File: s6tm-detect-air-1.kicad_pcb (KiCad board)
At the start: 2 copper layers, 67 x 67 mm, 82 parts, among them J1 Conn_01x04, J2 TC2030, J3 Conn_01x04, J4 Conn_01x04, J5 Conn_01x04_Pin, J6 Conn_01x08, SW1 SW_Push, SW2 SW_Push, U1 SYS1002-H2, U10 004-1-0100, U2 MiCS-5524, U3 LMC6482, U4 HT753-1, U5 SN65HVD230, U6 STM32F103C8Tx, U7 HTU21, U8 LM73100, U9 ENS16x, Y1 8M

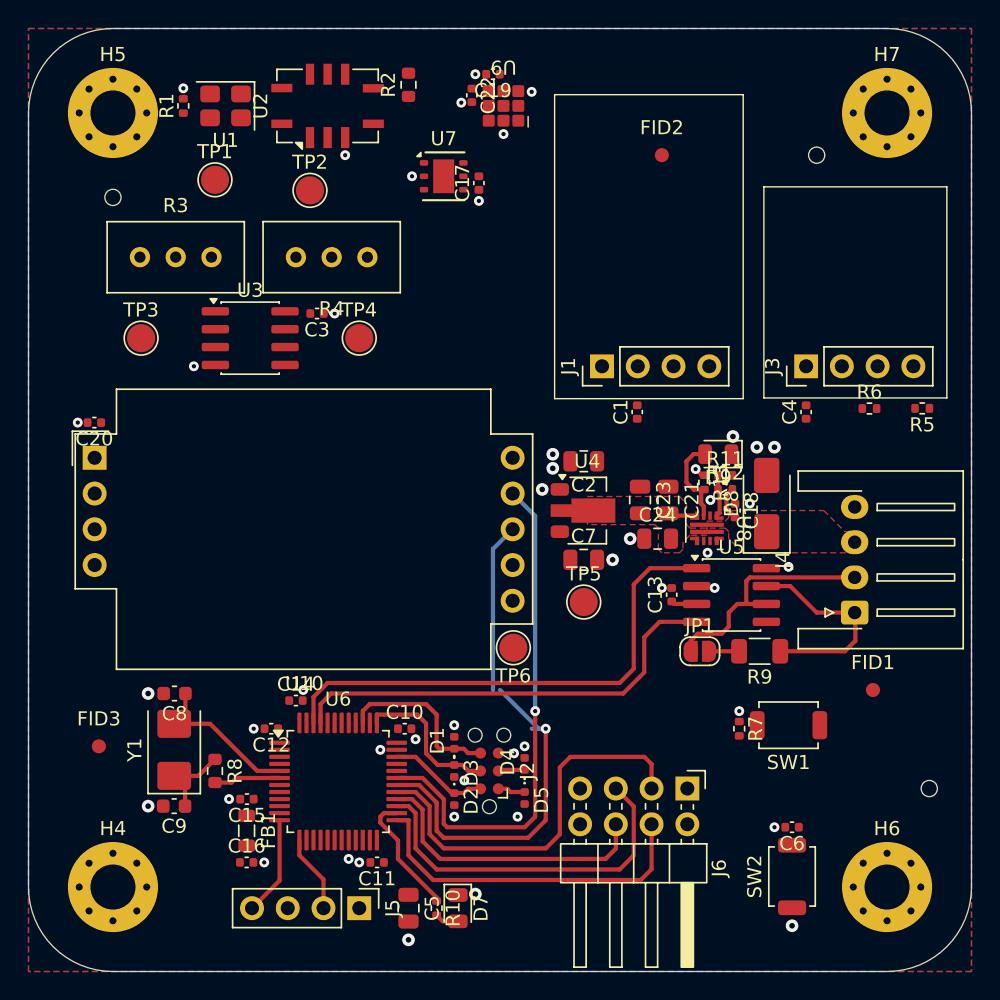
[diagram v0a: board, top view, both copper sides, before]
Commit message: pcb: add s88 cutout
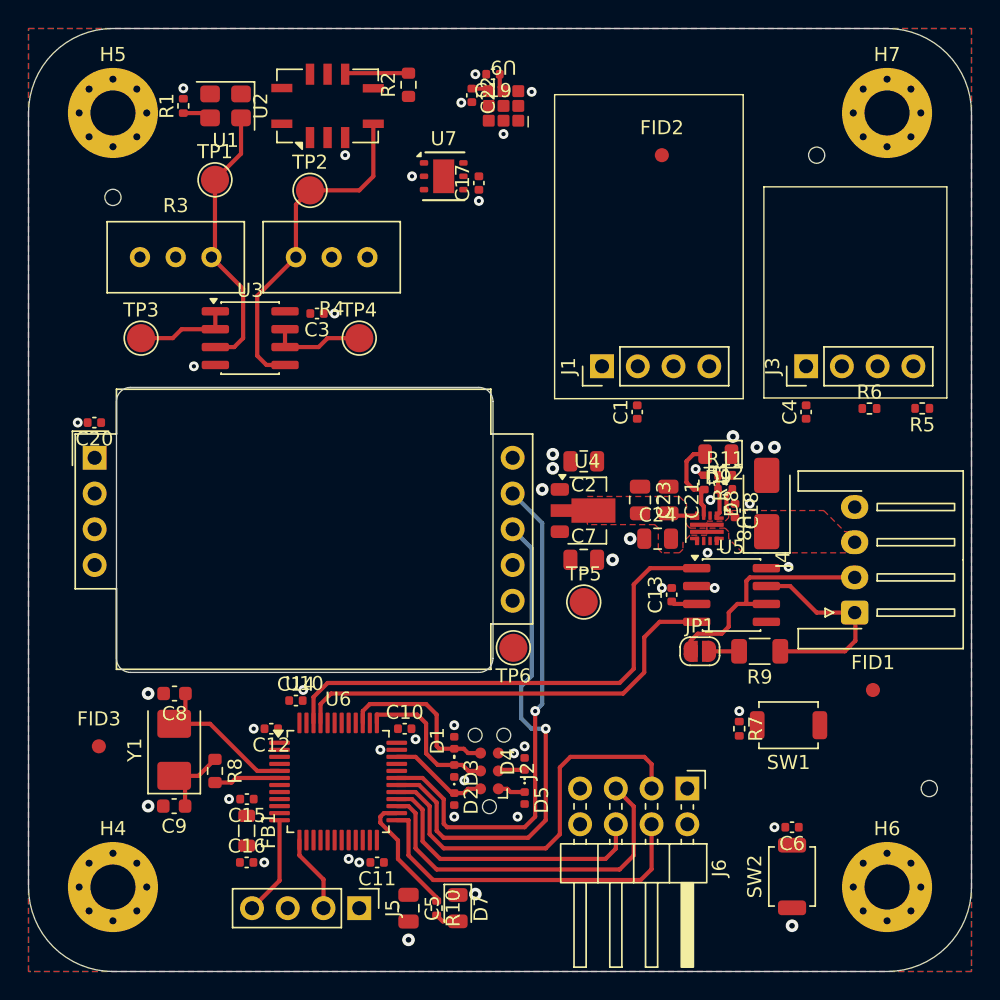
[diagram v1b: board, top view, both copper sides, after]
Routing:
- net Net-(U2-Rs1): track 0.00 -> 24.2 mm
- net Net-(U1-RS2): track 0.00 -> 19.7 mm
- net /RS_1: track 0.00 -> 6.81 mm
- net /RS_2: track 0.00 -> 6.81 mm
- net Net-(U2-Rh2): track 0.00 -> 4.53 mm
- net +3V3: track 4.60 -> 7.18 mm
- net Net-(U1-RH2): track 0.00 -> 2.04 mm
- net /S88_TX: track 37.2 -> 36.7 mm
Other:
- outline, holes or cut-outs redrawn

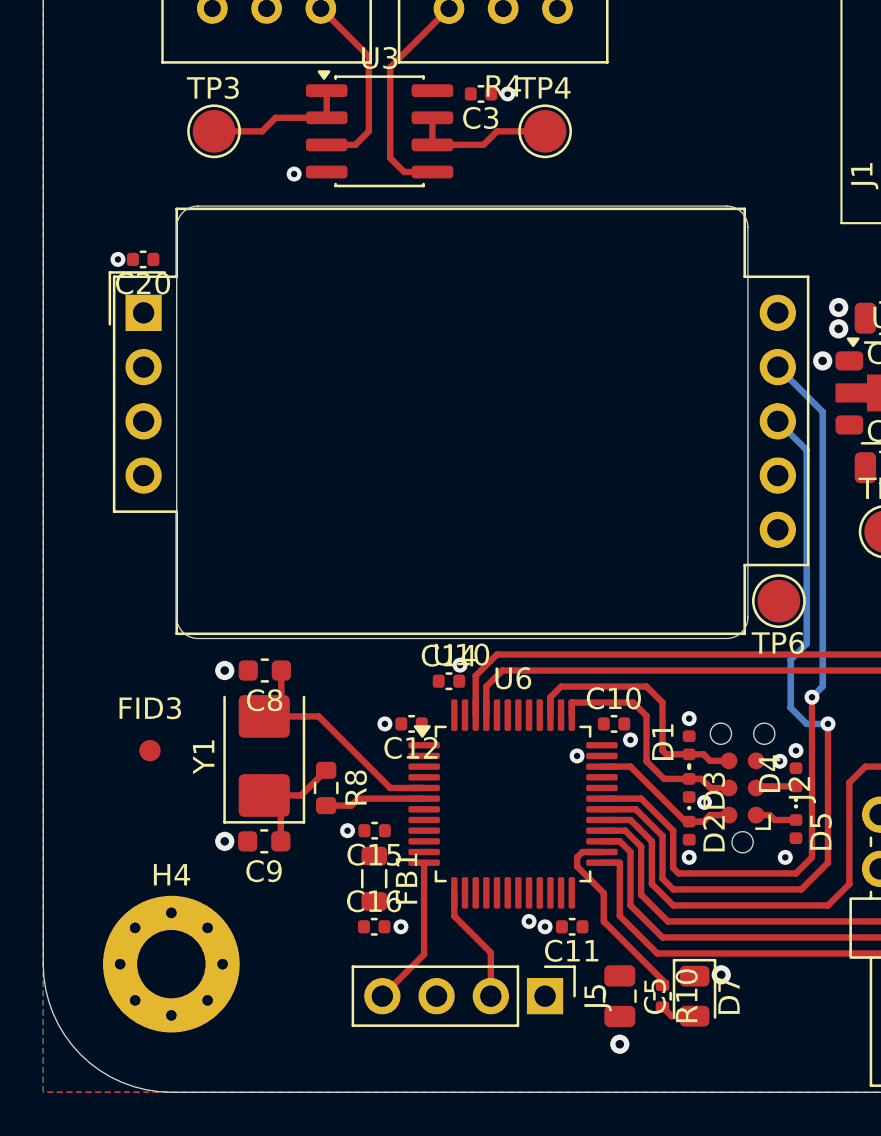
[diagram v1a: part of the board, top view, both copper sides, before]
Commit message: pcb: add mox sensors routing
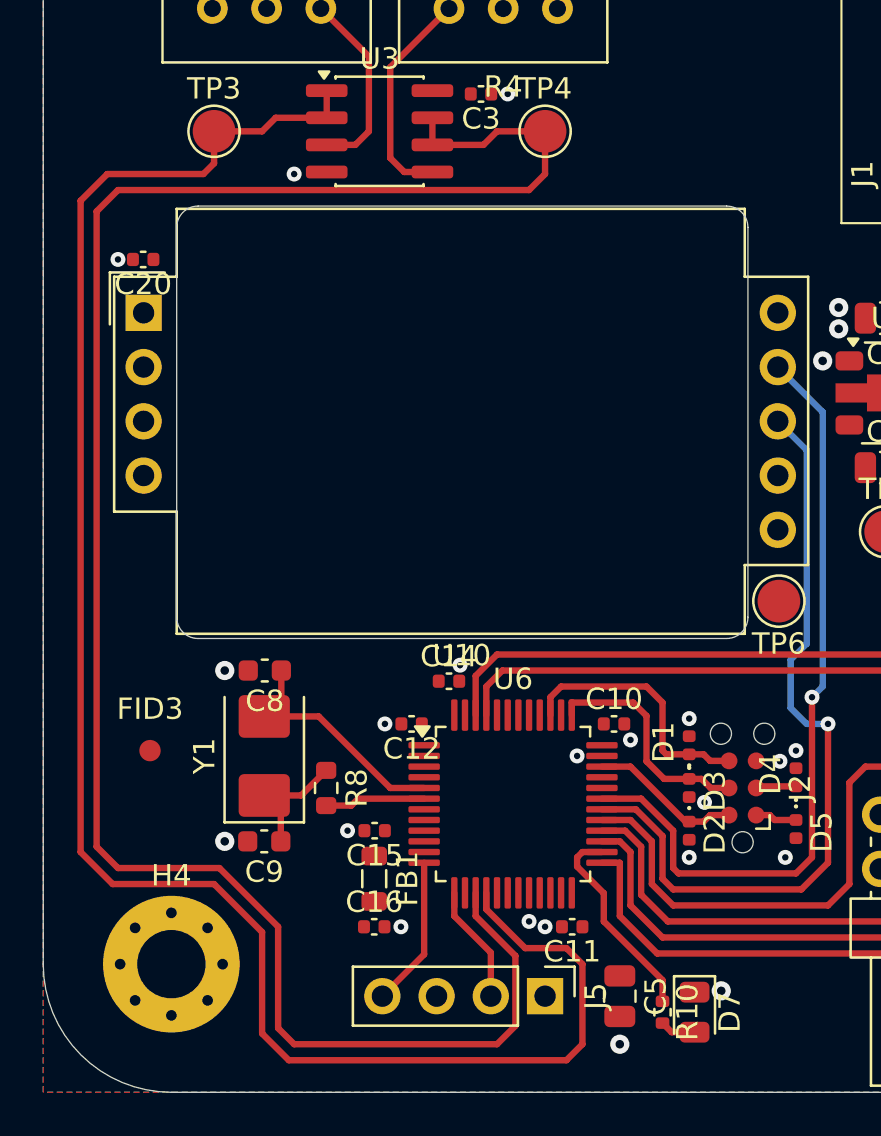
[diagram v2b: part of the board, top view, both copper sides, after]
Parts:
- moved D7 0.75 mm to (145.5, 116.2)
- moved R10 0.75 mm to (144.0, 116.2)
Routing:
- net /RS_1: track 6.81 -> 93.9 mm
- net /RS_2: track 6.81 -> 86.5 mm
- net Net-(U6-PB13): track 8.91 -> 9.66 mm

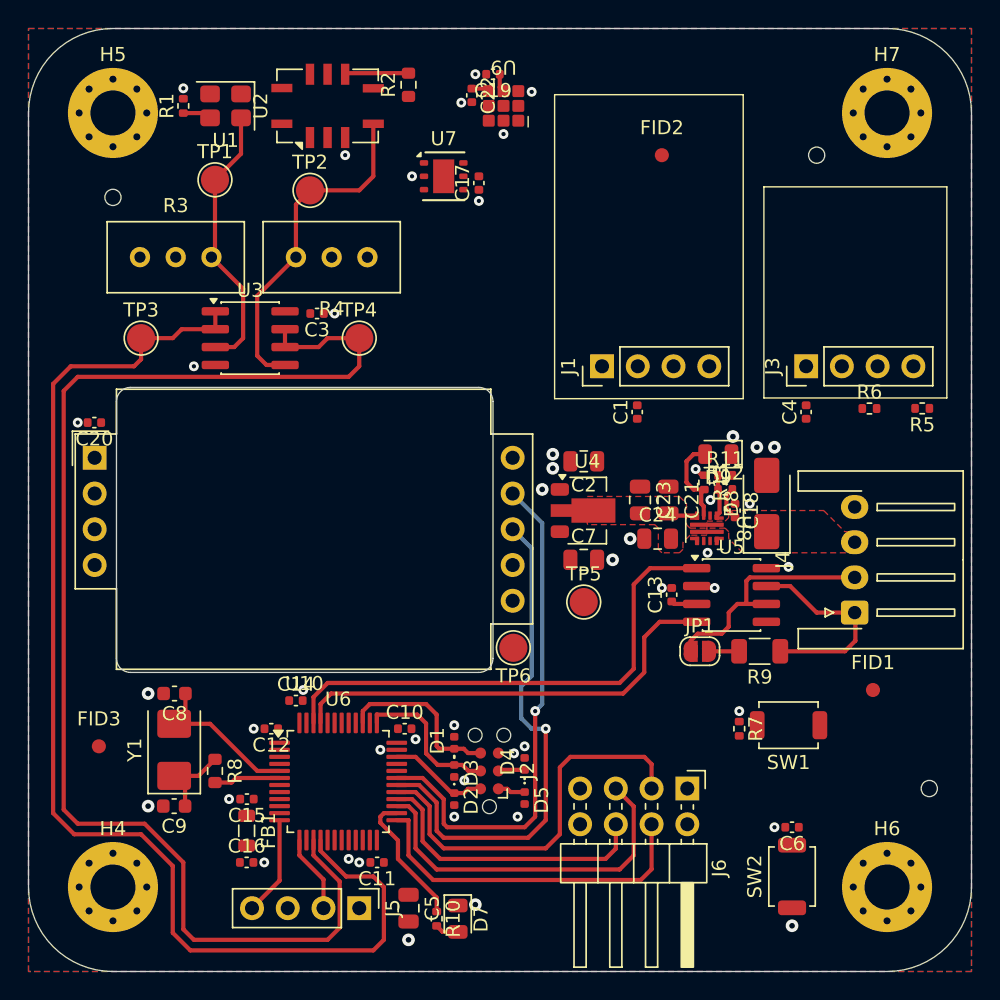
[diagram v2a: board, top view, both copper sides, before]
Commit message: pcb: add i2c routing
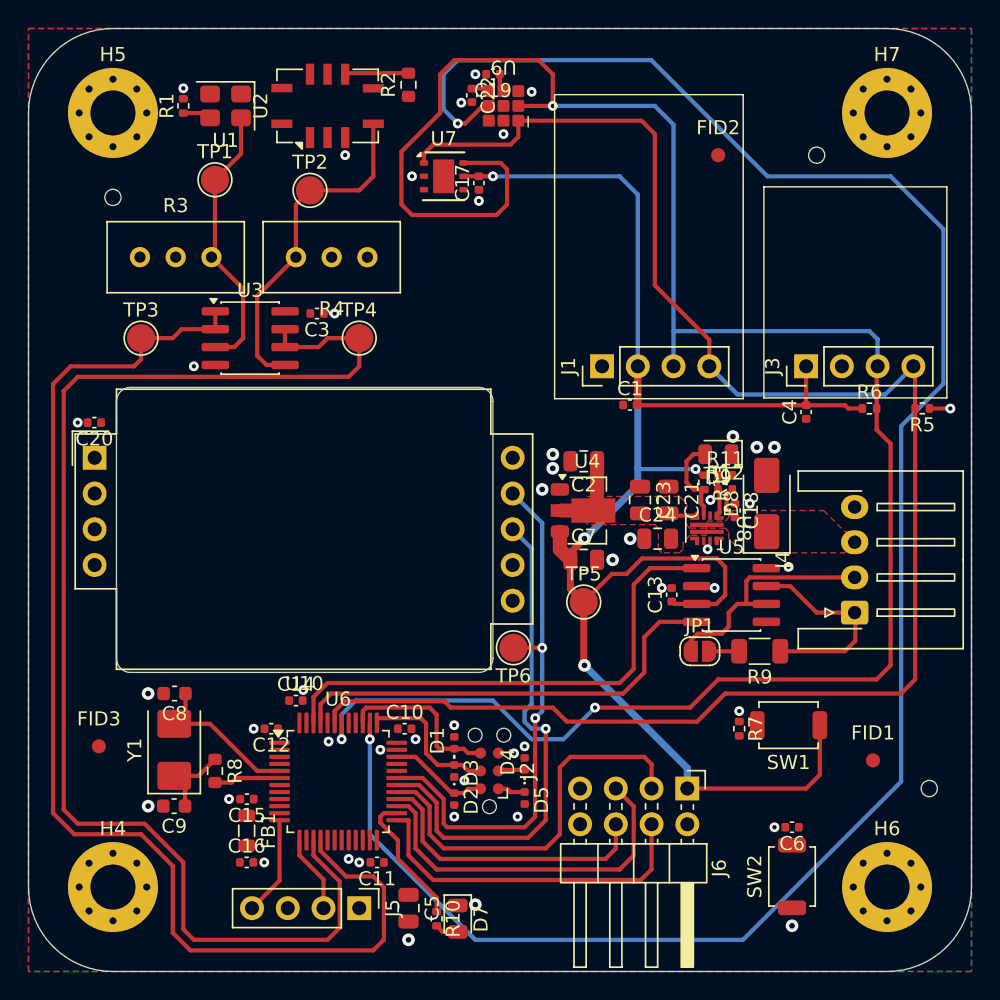
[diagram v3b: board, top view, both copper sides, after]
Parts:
- moved FID1 5.00 mm to (175.0, 105.0)
- moved FID2 4.00 mm to (164.0, 62.0)
- moved C1 0.72 mm to (157.7, 79.8), turned to 0 degrees
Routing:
- net /SCL: track 0.00 -> 148.1 mm, vias 0 -> 3
- net /~{ENS_INT}: track 0.00 -> 141.4 mm, vias 0 -> 2
- net /SDA: track 0.00 -> 119.9 mm
- net +3V3: track 7.18 -> 126.5 mm, vias 1 -> 5
- net +5V: track 2.11 -> 7.93 mm
- net /S88_RX: track 36.7 -> 38.7 mm, vias 1 -> 2
- net GND: vias 46 -> 47

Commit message: pcb: add +3V3 pwr routing
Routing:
- net +3V3: track 126.5 -> 304.0 mm, vias 5 -> 11
- net /NRST: track 1.90 -> 52.8 mm, vias 0 -> 3
- net Net-(U6-VDDA): track 0.00 -> 3.23 mm
- net GND: vias 47 -> 46

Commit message: pcb: add +5V pwr routing
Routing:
- net +5V: track 7.93 -> 85.4 mm, vias 0 -> 3
